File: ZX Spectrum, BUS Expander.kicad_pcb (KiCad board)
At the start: 2 copper layers, 90 x 87.4 mm, 16 parts, among them J1 SL-62, J2 Conn_02x28_Row_Letter_First

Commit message: Updated silk, fixed edge pcb dimensions a bit
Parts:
- added G***: LOGO, footprints:andy_karpov_logo4_silk, F.Cu at (142.5, 67.2)
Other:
- board text added: "Rev.A"

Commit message: Fixed Nemobus romcs signal
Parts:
- moved G*** 1.25 mm to (141.2, 67.0)
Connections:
- J1 pad B15: ~{RDR} -> ~{ROMCS}
- J1 pad B25: ~{ROMCS} -> unconnected-(J1-~{ROMCS}-PadB25)
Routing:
- net ~{ROMCS}: track 84.9 -> 114.3 mm, vias 0 -> 1
- net ~{RD}: track 84.8 -> 86.4 mm, vias 2 -> 4
- net ~{M1}: track 84.0 -> 85.5 mm, vias 2 -> 4
- net 12VAC: track 113.4 -> 114.9 mm, vias 4 -> 6
- net -5V: track 123.5 -> 125.0 mm, vias 3 -> 5
- net ~{WAIT}: track 89.4 -> 90.8 mm, vias 2 -> 4
- net +12V: track 133.7 -> 135.2 mm, vias 5 -> 7
- net ~{WR}: track 84.8 -> 86.1 mm, vias 2 -> 4
- net ~{HALT}: track 84.8 -> 85.9 mm, vias 2 -> 4
- net ~{MREQ}: track 84.8 -> 85.5 mm, vias 2 -> 4
- net ~{IORQ}: track 84.8 -> 85.2 mm, vias 2 -> 4
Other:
- board text added: "Modified by andykarpov 2024 Special Exclusive Kalantaj Edition"
- board text removed: "Modified by andykarpov 2024"

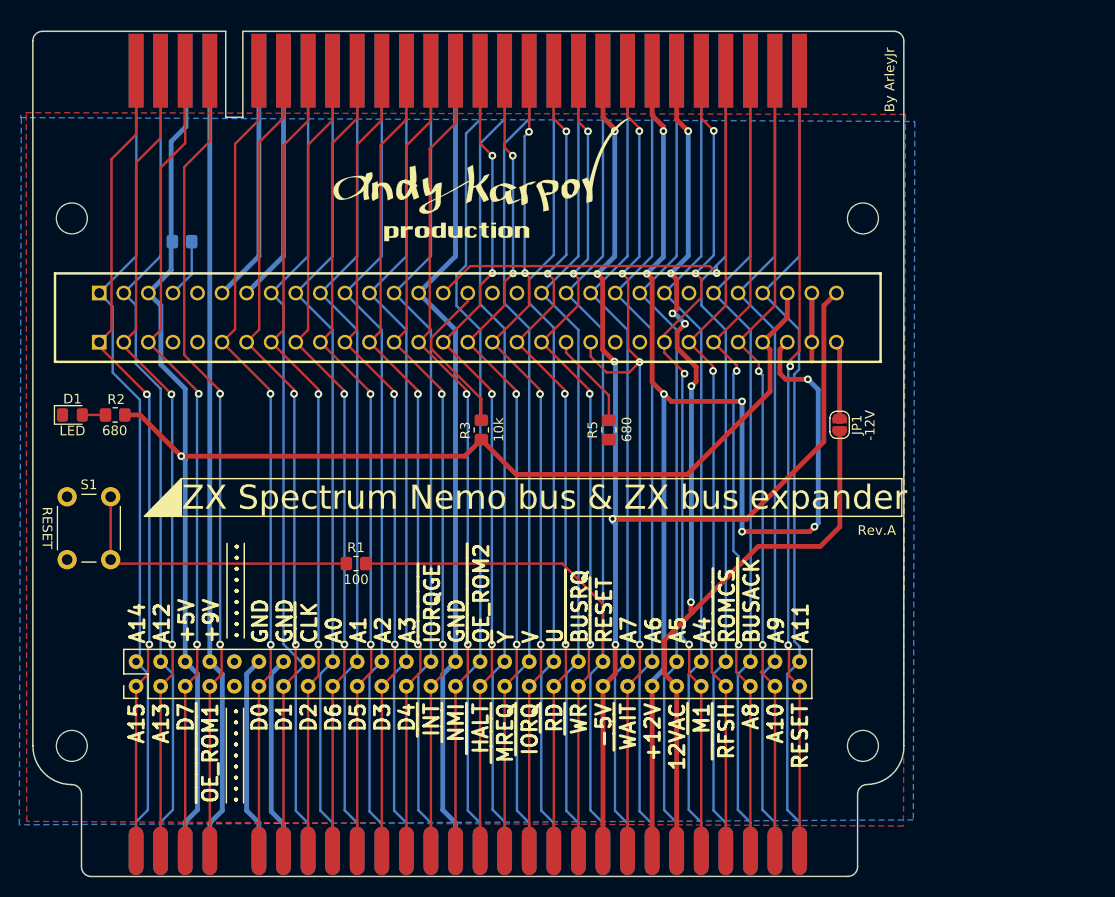
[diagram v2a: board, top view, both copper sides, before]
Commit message: Added more test points on nemobus slot
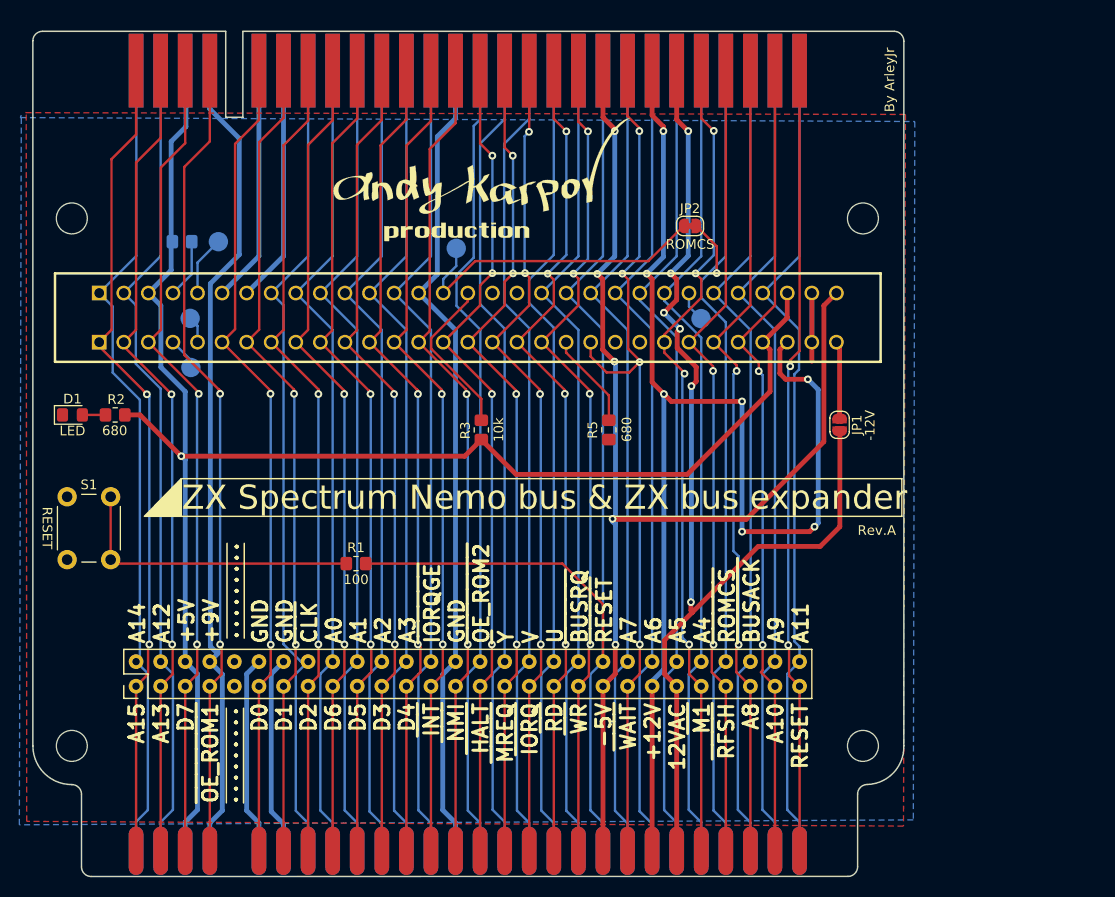
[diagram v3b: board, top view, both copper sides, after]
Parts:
- added JP2: ROMCS, Jumper:SolderJumper-2_P1.3mm_Bridged_RoundedPad1.0x1.5mm, F.Cu at (162.7, 71.8)
- added TP1: TestPoint, TestPoint:TestPoint_Pad_D2.0mm, B.Cu at (111.2, 86.4)
- added TP2: TestPoint, TestPoint:TestPoint_Pad_D2.0mm, B.Cu at (111.1, 81.4)
- added TP3: TestPoint, TestPoint:TestPoint_Pad_D2.0mm, B.Cu at (114.0, 73.4)
- added TP4: TestPoint, TestPoint:TestPoint_Pad_D2.0mm, B.Cu at (163.9, 81.4)
- added TP5: TestPoint, TestPoint:TestPoint_Pad_D2.0mm, B.Cu at (138.6, 74.1)
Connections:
- J1 pad A4: unconnected-(J1-BLK-PadA4) -> Net-(J1-BLK)
- J1 pad A5: unconnected-(J1-TURBO-PadA5) -> Net-(J1-TURBO)
- J1 pad B15: ~{ROMCS} -> Net-(J1-~{RDR})
- J1 pad B25: unconnected-(J1-~{ROMCS}-PadB25) -> Net-(J1-~{ROMCS})
- J1 pad B5: unconnected-(J1-F-PadB5) -> Net-(J1-F)
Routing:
- net Net-(J1-~{RDR}): track 0.00 -> 32.9 mm
- net ~{ROMCS}: track 114.3 -> 90.3 mm
- net Net-(J1-F): track 0.00 -> 6.20 mm
- net Net-(J1-BLK): track 0.00 -> 3.38 mm
- net +9V: track 81.7 -> 85.1 mm
- net Net-(J1-~{ROMCS}): track 0.00 -> 3.16 mm
- net Net-(J1-TURBO): track 0.00 -> 2.78 mm

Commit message: Added more leds
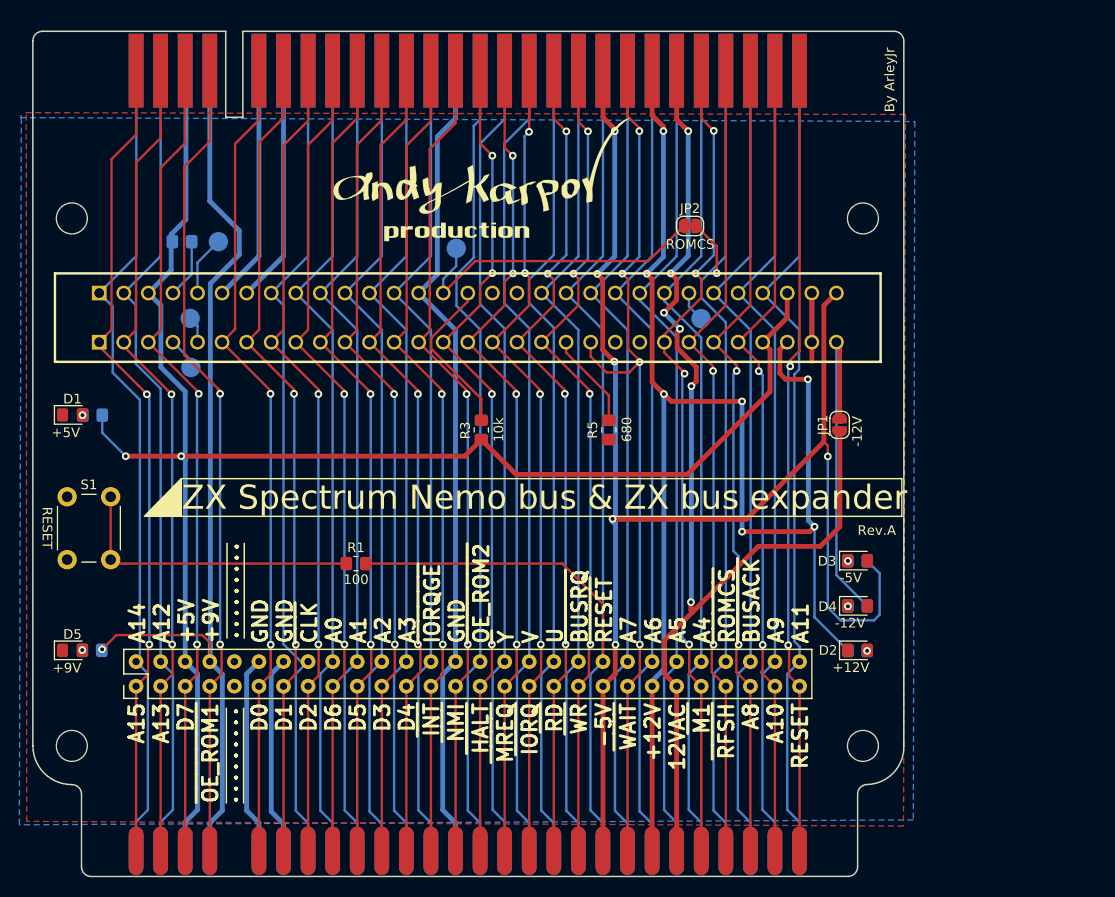
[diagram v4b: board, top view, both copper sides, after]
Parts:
- added D2: +12V, LED_SMD:LED_0805_2012Metric_Pad1.15x1.40mm_HandSolder, F.Cu at (180.1, 115.7)
- added D3: -5V, LED_SMD:LED_0805_2012Metric_Pad1.15x1.40mm_HandSolder, F.Cu at (180.1, 106.4)
- added D4: -12V, LED_SMD:LED_0805_2012Metric_Pad1.15x1.40mm_HandSolder, F.Cu at (180.1, 111.1)
- added D5: +9V, LED_SMD:LED_0805_2012Metric_Pad1.15x1.40mm_HandSolder, F.Cu at (98.9, 115.7)
- added R6: 1k, Resistor_SMD:R_0805_2012Metric_Pad1.20x1.40mm_HandSolder, B.Cu at (180.1, 115.7)
- added R7: 680, Resistor_SMD:R_0805_2012Metric_Pad1.20x1.40mm_HandSolder, B.Cu at (180.1, 106.4)
- added R8: 1k, Resistor_SMD:R_0805_2012Metric_Pad1.20x1.40mm_HandSolder, B.Cu at (180.1, 111.1)
- added R9: 680, Resistor_SMD:R_0805_2012Metric_Pad1.20x1.40mm_HandSolder, B.Cu at (100.9, 115.7)
- D1: value LED -> +5V
- R2: moved to B.Cu
- moved R2 2.34 mm to (101.0, 91.4)
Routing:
- net -5V: track 125.0 -> 154.6 mm, vias 5 -> 6
- net -12V: track 8.03 -> 36.6 mm
- net +12V: track 135.2 -> 149.1 mm
- net +9V: track 85.1 -> 98.4 mm, vias 0 -> 1
- net +5V: track 171.2 -> 174.6 mm, vias 1 -> 2
- net Net-(D1-A): track 2.39 -> 0.07 mm, vias 0 -> 1
- net Net-(D4-K): track 0.00 -> 0.12 mm, vias 0 -> 1
- net Net-(D2-A): track 0.00 -> 0.09 mm, vias 0 -> 1
- net Net-(D3-K): track 0.00 -> 0.05 mm, vias 0 -> 1
- net Net-(D5-A): track 0.00 -> 0.03 mm, vias 0 -> 1
